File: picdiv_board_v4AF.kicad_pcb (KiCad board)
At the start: 2 copper layers, 100 x 99.5 mm, 81 parts, among them J1 DC-Input, J10 PPS_B, J11 PPS_B, J2 MountingHole_M2.5, J3 MountingHole_M2.5, J4 TEST_1PPS, J5 Conn_01x06, J6 Sync, J7 Sync, J8 10MHz, J9 10MHz, SW1 SW_DIP_x03, U1 LT1963AEST-3.3, U10 74HC14, U2 LT1963AEST-3.3, U3 PIC12F675-xSN, U4 NE555D, U5 IDT5PB1108, U6 IDT5PB1108, U7 LT1963AEQ, U8 ADR4540

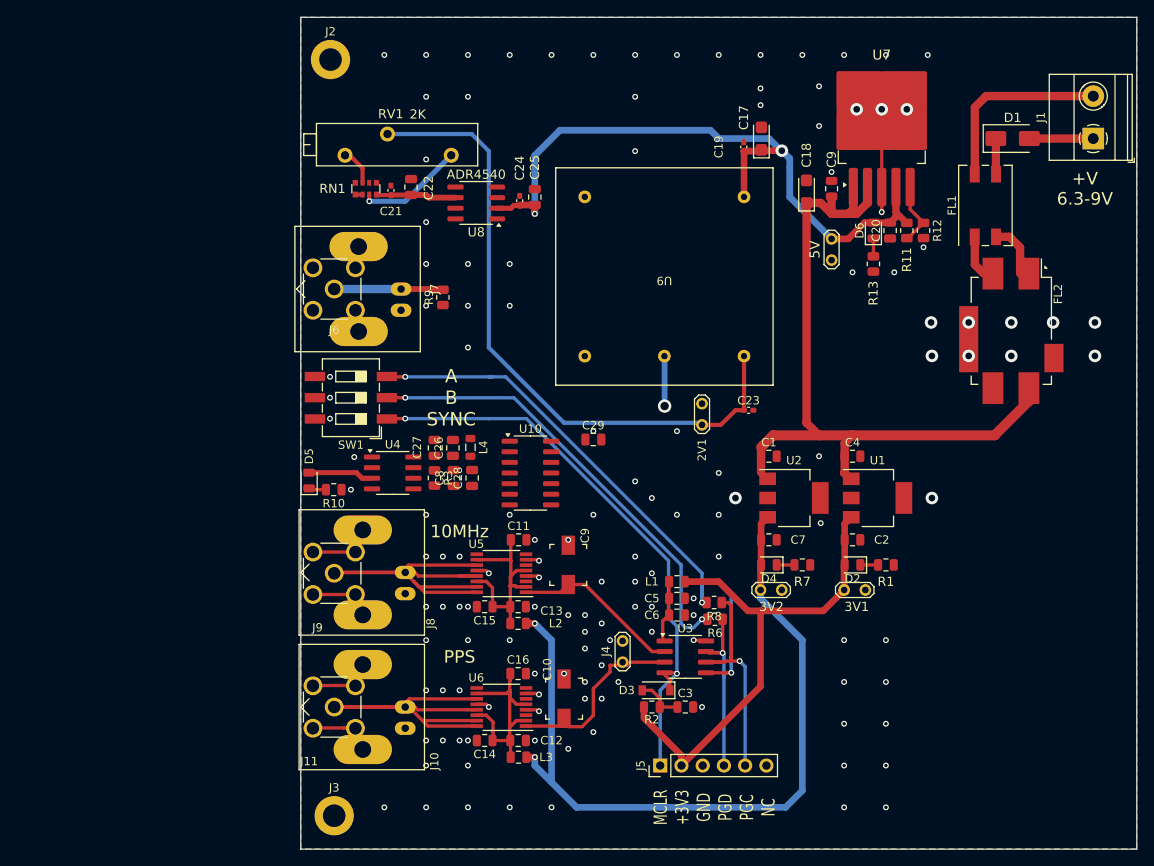
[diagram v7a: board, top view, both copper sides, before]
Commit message: Start fixing JLC design rule violations. There over 100 left.
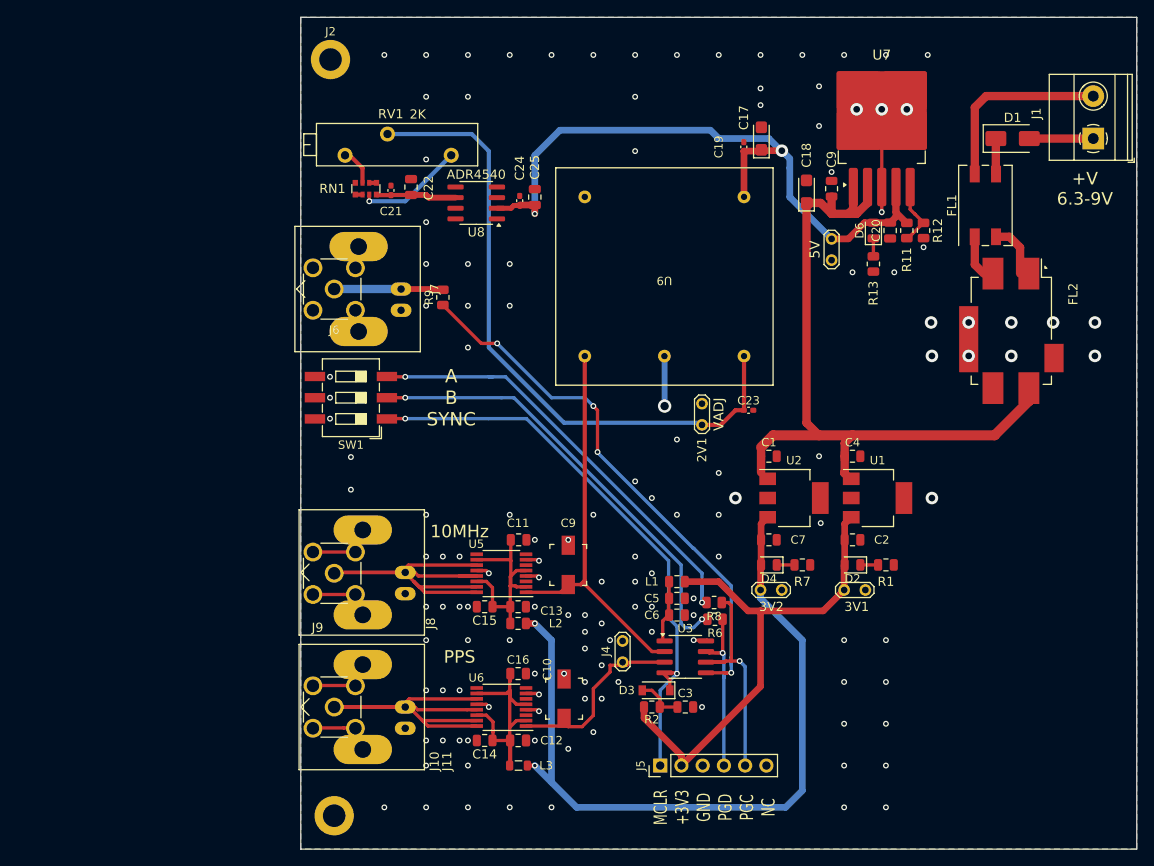
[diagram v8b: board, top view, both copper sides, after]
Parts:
- removed C26, C27, C28, C29: 100n, Capacitor_SMD:C_0805_2012Metric
- removed C8: 1µF, Capacitor_SMD:C_0805_2012Metric
- removed D5: PPS_BLINK, LED_SMD:LED_0805_2012Metric
- removed L4: 2u2, Inductor_SMD:L_0805_2012Metric
- removed R10: 100R, Resistor_SMD:R_0805_2012Metric
- removed R3: 1.8K, Resistor_SMD:R_0805_2012Metric
- removed U10: 74HC14, Package_SO:SOIC-14_3.9x8.7mm_P1.27mm
- removed U4: NE555D, Package_SO:SOIC-8_3.9x4.9mm_P1.27mm
- moved L3 1.00 mm to (151.1, 140.0)
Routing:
- net /sync: track 13.5 -> 66.0 mm, vias 1 -> 4
- net 10MHz: track 20.1 -> 47.6 mm
- net Net-(D5-A): track 7.80 -> 0.00 mm
- net Net-(D5-K): track 2.00 -> 0.00 mm
- net /U6_3V3: track 26.7 -> 27.9 mm
- net 3V3_OUT: track 92.9 -> 91.8 mm
- net Net-(RN1-R1.1): track 0.00 -> 0.87 mm
- net GND: vias 139 -> 138
